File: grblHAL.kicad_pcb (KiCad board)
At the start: 2 copper layers, 48 parts, among them J1 Conn_01x03, J2 Conn_02x08_Odd_Even, J3 Conn_01x06, J4 Conn_01x06, J5 Conn_01x04, U1 YAAJ_BluePill_Part_Like_SWD_B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, U10 PC817, U11 PC817, U12 PC817, U13 PC817, U14 LM1117-3.3, U2 TMC2208_SILENTSTEPSTICK, U4 PC817, U5 PC817, U6 PC817, U7 PC817, U8 PC817, U9 PC817

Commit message: Schematic Layout Nets Opto 4 TMC Stage 2
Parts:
- added C3: 100uF/35v, Capacitor_THT:CP_Radial_D8.0mm_P3.50mm, F.Cu at (156.1, 60.1)
- added C4: 100uF/35v, Capacitor_THT:CP_Radial_D8.0mm_P3.50mm, F.Cu at (156.2, 130.1)
- added J6: Conn_01x04, Connector_PinHeader_2.54mm:PinHeader_1x04_P2.54mm_Vertical, F.Cu at (166.9, 83.7)
- added J7: Conn_01x04, Connector_PinHeader_2.54mm:PinHeader_1x04_P2.54mm_Vertical, F.Cu at (166.9, 105.3)
- added J8: Conn_01x04, Connector_PinHeader_2.54mm:PinHeader_1x04_P2.54mm_Vertical, F.Cu at (166.9, 126.7)
- added U15: TMC2208, TMC2208_SILENTSTEPSTICK:MODULE_TMC2208_SILENTSTEPSTICK, F.Cu at (154.4, 87.6)
- added U16: TMC2208, TMC2208_SILENTSTEPSTICK:MODULE_TMC2208_SILENTSTEPSTICK, F.Cu at (154.4, 109.1)
- added U17: TMC2208, TMC2208_SILENTSTEPSTICK:MODULE_TMC2208_SILENTSTEPSTICK, F.Cu at (154.3, 130.5)
- added U3: buck2596, DC_DC_LM2596_small:DC_DC_LM2596_small, F.Cu at (91.0, 134.0)
- C1, C2, D1, D10, D11, D12, D13, D2, D3, D4, D5, D6, D7, D8, D9, R1, R10, R11, R12, R13, R2, R3, R4, R5, R6, R7, R8, R9, U14: moved to B.Cu
- J2: value Conn_02x08_Odd_Even -> Conn
- J3, J4: footprint Connector_Phoenix_MC_HighVoltage:PhoenixContact_MC_1,5_6-G-5.08_1x06_P5.08mm_Horizontal -> Connector_Phoenix_MSTB:PhoenixContact_MSTBA_2,5_6-G-5,08_1x06_P5.08mm_Horizontal
- U2: value TMC2208_SILENTSTEPSTICK -> TMC2208
- moved JP1 70.7 mm to (141.1, 57.1)
- moved C2 36.5 mm to (96.6, 136.2), turned to -90 degrees
- moved J1 36.2 mm to (60.5, 131.9), turned to -90 degrees
- moved D1 36.1 mm to (69.0, 131.9), turned to 180 degrees
- moved U14 34.4 mm to (89.7, 134.6)
- moved D12 23.7 mm to (107.0, 121.1)
- moved C1 23.4 mm to (96.6, 130.8), turned to -90 degrees
- moved TP1 17.8 mm to (123.7, 141.9)
- moved R13 17.7 mm to (101.7, 121.1), turned to 0 degrees
- moved U2 8.18 mm to (154.4, 66.0)
- moved J5 7.98 mm to (166.9, 62.2)
- moved J4 1.77 mm to (60.5, 95.2)
- moved D13 1.58 mm to (94.5, 95.9), turned to 180 degrees
- moved R12 0.87 mm to (94.5, 98.5)
- moved R1 0.43 mm to (95.2, 78.1)
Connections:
- C1 pad 2: 5V -> GND
- C2 pad 2: 5V -> GND
- JP1 pad 1: 5V -> GND
- JP1 pad 2: EN -> STEN
- R12 pad 1: 5V -> GND
- R13 pad 1: 5V -> GND
- U1 pad 19: 5V -> GND
- U1 pad 39: 5V -> GND
- U10 pad 3: 5V -> GND
- U11 pad 3: 5V -> GND
- U12 pad 3: 5V -> GND
- U13 pad 3: 5V -> GND
- U14 pad 1: 5V -> GND
- U2 pad JP1_8: EN -> STEN
- U2 pad JP2_2: 5V -> GND
- U2 pad JP2_8: 5V -> GND
- U4 pad 3: 5V -> GND
- U5 pad 3: 5V -> GND
- U6 pad 3: 5V -> GND
- U7 pad 3: 5V -> GND
- U8 pad 3: 5V -> GND
- U9 pad 3: 5V -> GND
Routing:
- net GND: track 0.00 -> 275.7 mm, vias 0 -> 6
- net VM: track 0.00 -> 192.7 mm, vias 0 -> 2
- net Net-(J4-Pad5): track 0.00 -> 88.4 mm
- net 3V3: track 0.00 -> 74.8 mm, vias 0 -> 7
- net Net-(J1-Pad3): track 0.00 -> 69.3 mm
- net 5V: track 0.00 -> 31.9 mm
- net Net-(D1-Pad1): track 0.00 -> 15.6 mm
- net Net-(J1-Pad2): track 0.00 -> 9.79 mm
- net Net-(D1-Pad2): track 0.00 -> 6.55 mm
- net Net-(D12-Pad1): track 0.00 -> 2.30 mm
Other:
- board outline added: 116 x 96.7 mm

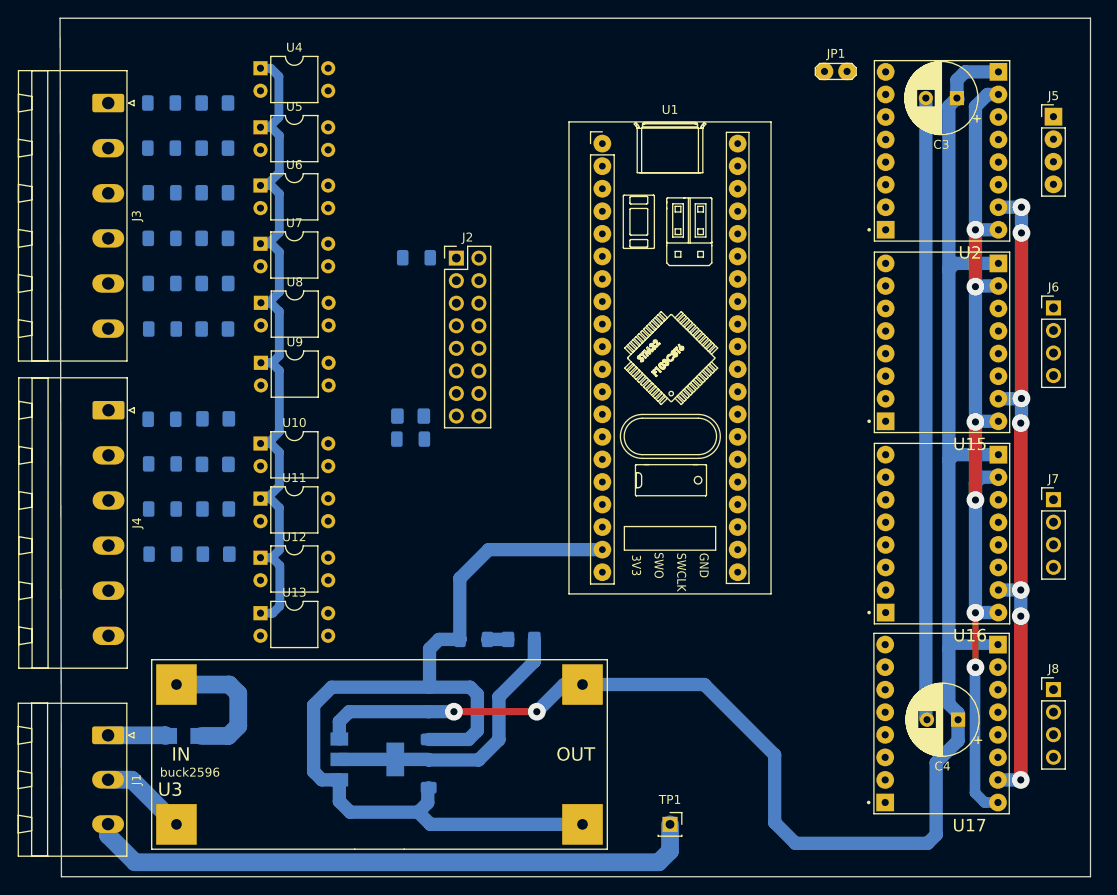
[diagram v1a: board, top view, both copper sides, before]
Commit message: Schematic Full Layout Nets Opto Connector 4-TMC Stage 3
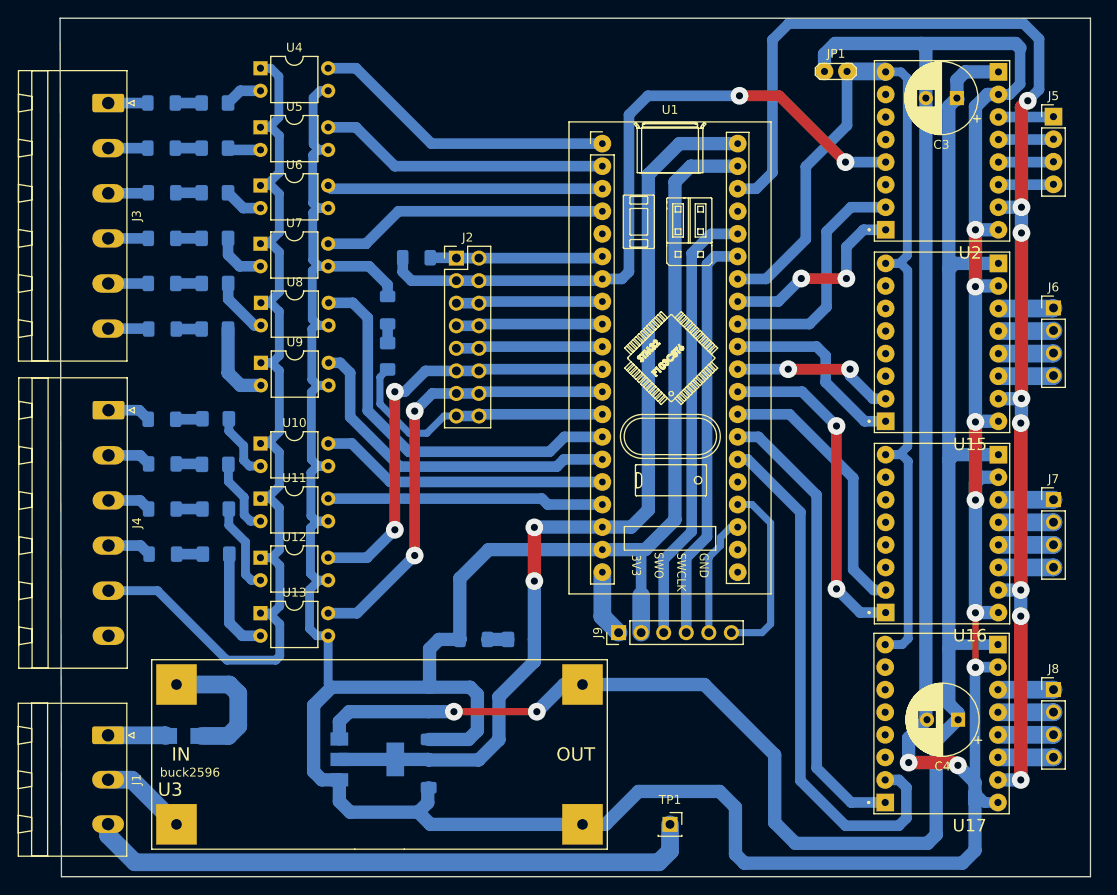
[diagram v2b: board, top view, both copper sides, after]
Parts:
- added J9: Conn_01x06, Connector_PinHeader_2.54mm:PinHeader_1x06_P2.54mm_Vertical, F.Cu at (118.0, 120.3)
- moved R12 14.7 mm to (91.9, 84.0), turned to -90 degrees
- moved D13 7.22 mm to (91.9, 89.2), turned to -90 degrees
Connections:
- U1 pad 18: unconnected-(U1-Pad18) -> 5V
- U1 pad 20: unconnected-(U1-Pad20) -> Net-(U1-Pad20)
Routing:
- net GND: track 275.7 -> 559.4 mm, vias 6 -> 8
- net STEN: track 0.00 -> 111.4 mm
- net UART1_PDN1: track 0.00 -> 78.5 mm, vias 0 -> 2
- net 5V: track 31.9 -> 107.4 mm, vias 0 -> 2
- net 3V3: track 74.8 -> 145.7 mm, vias 7 -> 8
- net STEPX: track 0.00 -> 60.3 mm
- net DIRX: track 0.00 -> 51.7 mm
- net OXY02: track 0.00 -> 50.7 mm, vias 0 -> 2
- net SPDIR: track 0.00 -> 50.2 mm
- net OXY01: track 0.00 -> 48.8 mm, vias 0 -> 2
- net SPEN: track 0.00 -> 46.3 mm
- net ESTOP: track 0.00 -> 44.6 mm
- net HOLD: track 0.00 -> 38.9 mm
- net DIRY: track 0.00 -> 37.7 mm, vias 0 -> 2
- net LIMX: track 0.00 -> 34.4 mm
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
